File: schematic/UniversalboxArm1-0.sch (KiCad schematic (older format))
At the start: 170 parts, among them J1 USB_B_Micro, J110 Conn_01x03_Male, J120 Conn_02x04_Counter_Clockwise, J121 Conn_01x02_Male, J20 AVR-ISP-6, J50 Conn_01x14_Female, J60 Conn_01x06_Female, J61 Conn_02x08_Odd_Even, J62 Conn_02x04_Odd_Even, J90 Conn_02x03_Odd_Even, J91 Conn_02x04_Odd_Even, K90 IM01, K91 IM01, K92 IM01, K93 IM01, Q120 IRLML6402, Q20 BCX56-16, Q21 BSS138, Q22 BSS138, Q23 IRLML6402, Q24 IRLML6402, Q25 BSS138, Q50 IRLML6402, Q51 IRLML6402, Q60 BSS138, Q61 BSS138, Q62 BSS138, Q90 BSS138, Q91 BSS138, Q92 BSS138, Q93 BSS138, SW60 SW_SPST, SW61 SW_SPST, SW62 SW_SPST, SW63 SW_SPST, U1 USBLC6-2SC6, U110 MAX3221, U130 TSOP312xx, U2 LP38693MP-3.3, U20 ATtiny861A-SU, U21 REF3020, U22 MCP6542, U50 AT45DB641-S, U60 STM32L452RETx, U61 MCP65R41T-1202E, Y60 16MHz, Y61 32768Hz

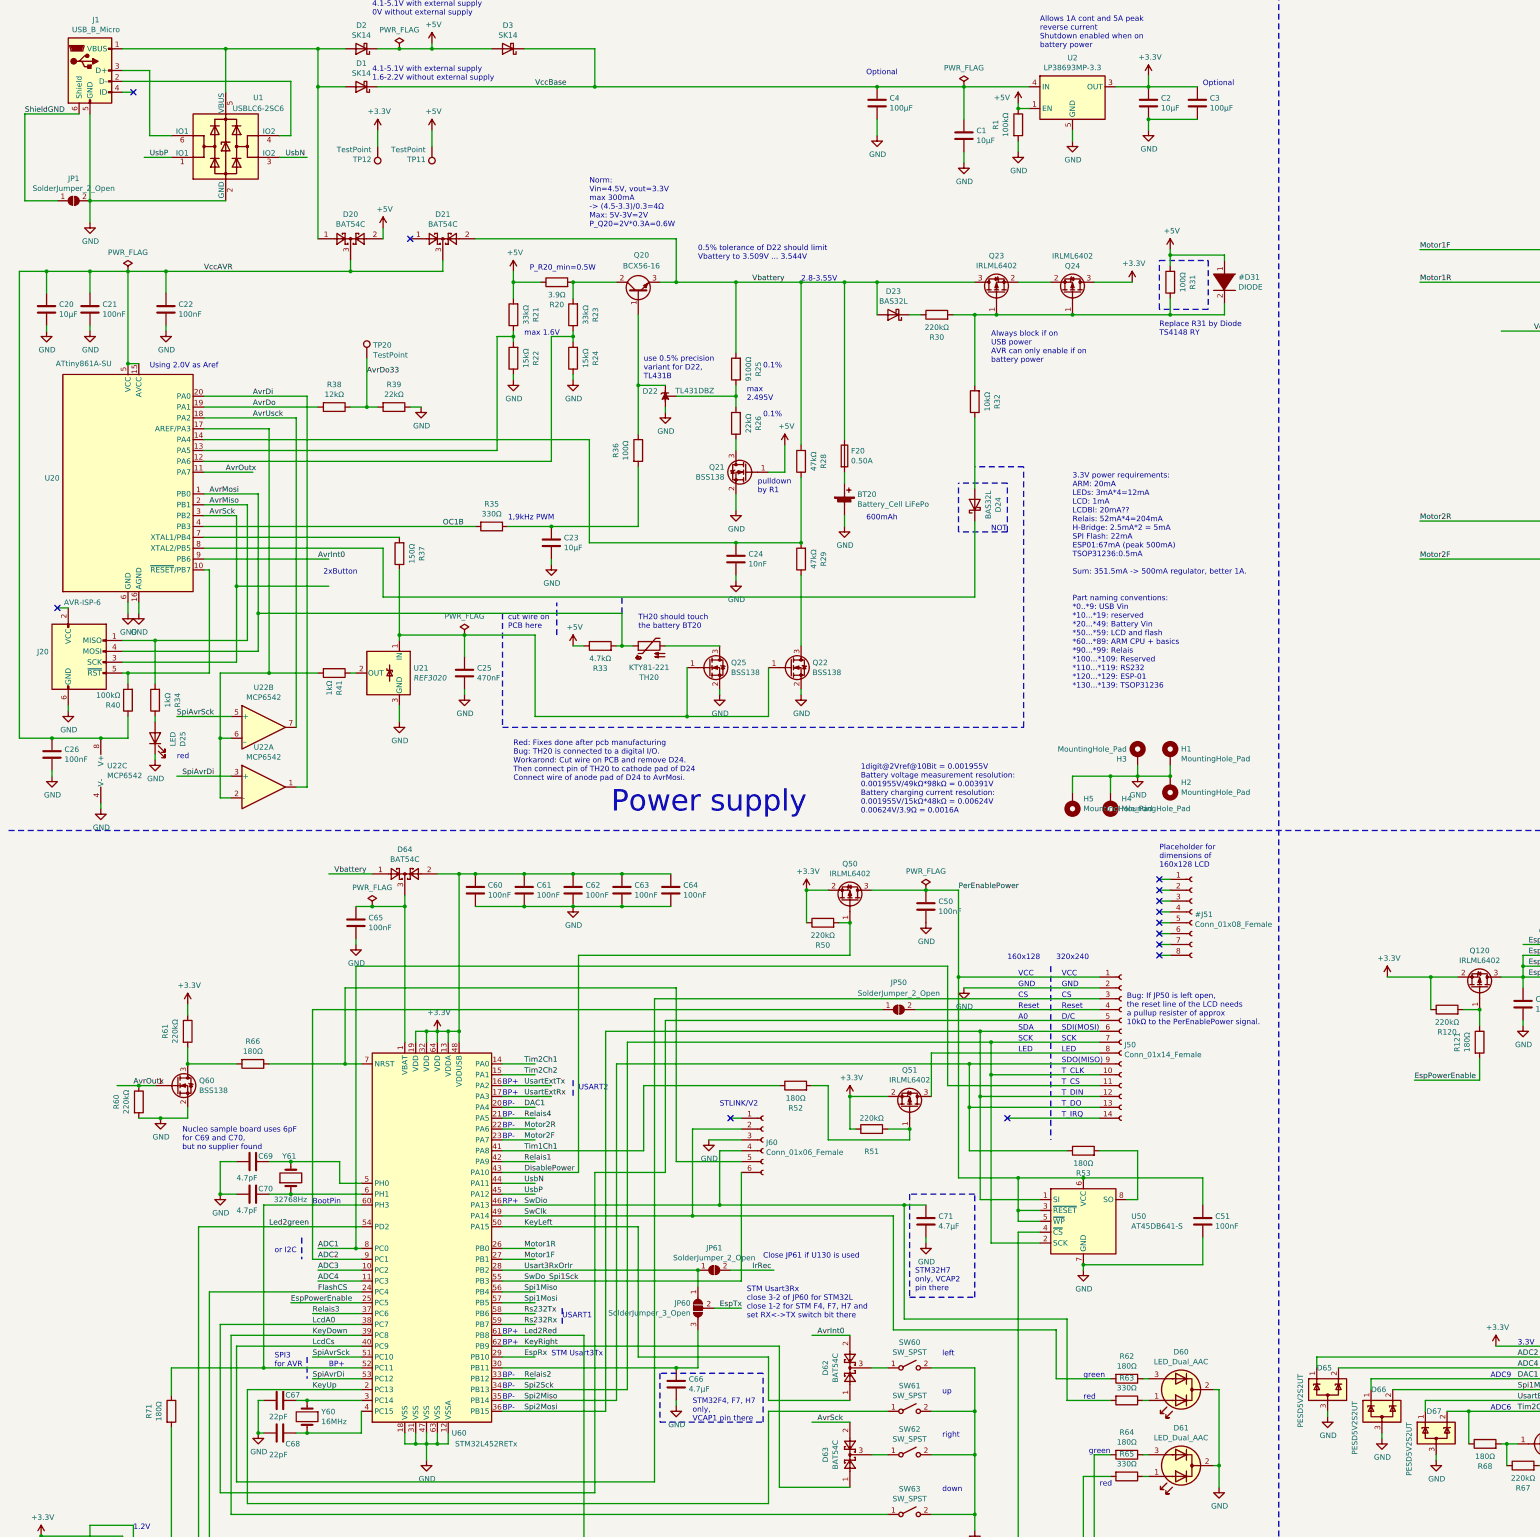
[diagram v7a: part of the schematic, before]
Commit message: Schematic: Revision 0.8 Workaround for issues with the crystals Reduce the value of two resistors
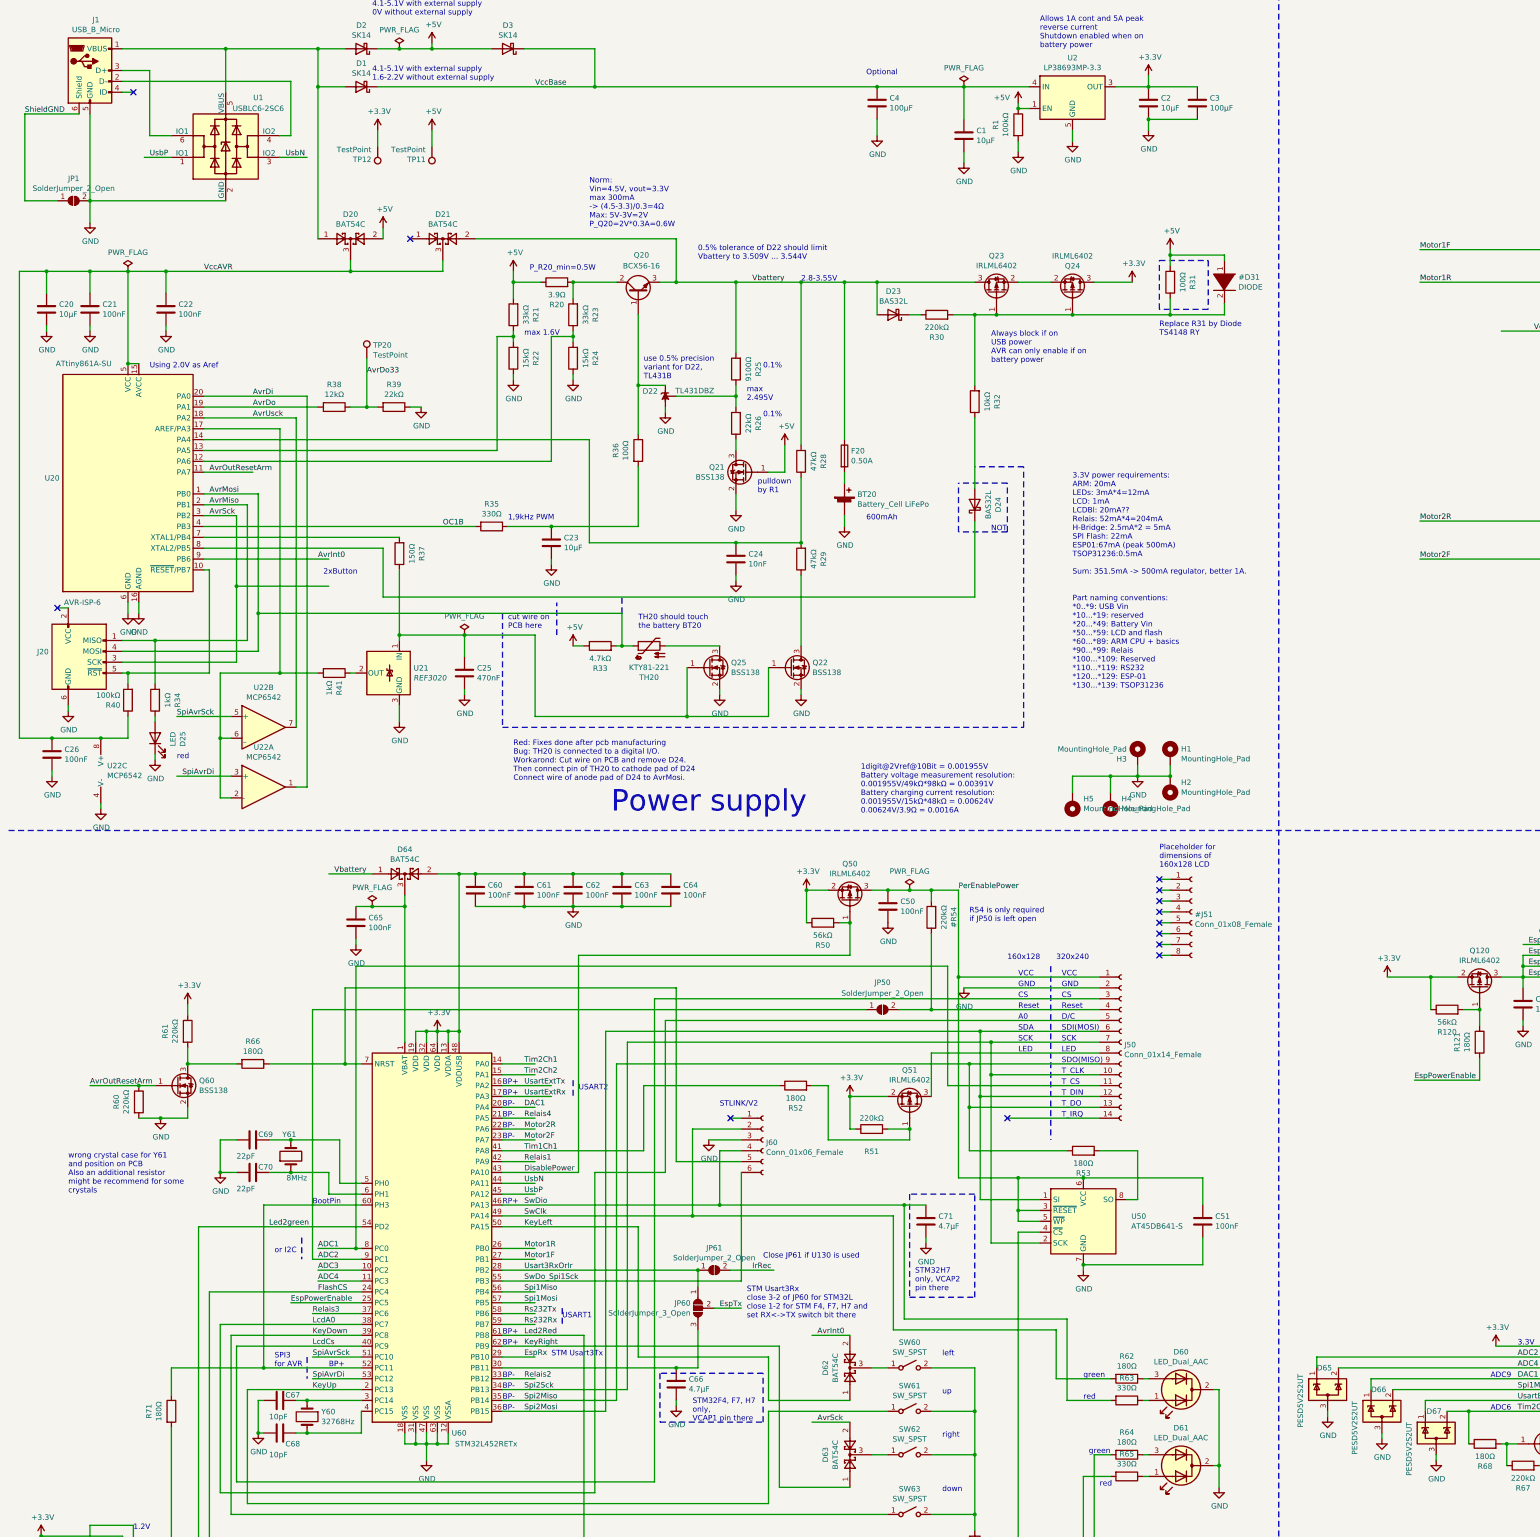
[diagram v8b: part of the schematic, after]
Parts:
- C67, C68: value 22pF -> 10pF
- C69, C70: value 4.7pF -> 22pF
- R120, R50: value 220kΩ -> 56kΩ
- Y60: value 16MHz -> 32768Hz
- Y61: value 32768Hz -> 8MHz
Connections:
- net labels added: 220kΩ, AvrOutResetArm
- net labels removed: AvrOutx
- wire segments 758 -> 765
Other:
- note added: "R54 is only required \nif JP50 is left open"
- note added: "wrong crystal case for Y61\nand position on PCB\nAlso an additional resistor\nmight be recommend for some\ncrystals"
- note removed: "Bug: If JP50 is left open,\nthe reset line of the LCD needs\na pullup resister of approx\n10kΩ to the PerEnablePower signal."
- note removed: "Nucleo sample board uses 6pF\nfor C69 and C70,\nbut no supplier found"
- moved on the sheet: C50, C69, C70, JP50, Y61
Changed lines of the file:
@@
 Sheet 1 1
 Title ""
-Date "2022-01-02"
-Rev "0.7"
+Date "2022-01-17"
+Rev "0.8"
 Comp ""
 Comment1 ""
@@
 	4700 7000 4700 6950
 Wire Wire Line
-	2900 6800 2900 4550
-Wire Wire Line
-	2300 4550 2900 4550
-Wire Wire Line
 	2350 5850 2350 6800
 Wire Wire Line
@@
 Wire Wire Line
 	2300 4950 2750 4950
-Text Label 2500 4950 0    50   ~ 0
-AvrOutx
+Text Label 2350 4950 0    50   ~ 0
+AvrOutResetArm
 $Comp
 L Connector:TestPoint TP20
@@
 $EndComp
 Wire Wire Line
-	3350 6800 2900 6800
+	3350 6800 3000 6800
 NoConn ~ 1650 1450
 Wire Wire Line
@@
 	2450 7400 2550 7400
 Wire Wire Line
-	2900 6800 2450 6800
-Wire Wire Line
 	2450 6800 2450 7400
-Connection ~ 2900 6800
 Connection ~ 2450 7400
 Text Label 2050 7200 0    50   ~ 0
@@
 Wire Wire Line
 	1850 10600 1700 10600
-Text Label 1650 10600 0    50   ~ 0
-AvrOutx
+Text Label 1250 10600 0    50   ~ 0
+AvrOutResetArm
 $Comp
 L Device:R R61
@@
 Connection ~ 1700 10600
 Wire Wire Line
-	1700 10600 1500 10600
-Wire Wire Line
 	2150 10800 2150 10900
 Wire Wire Line
@@
 P 3250 13650
 F 0 "Y60" V 3204 13781 50  0000 L CNN
-F 1 "16MHz" V 3295 13781 50  0000 L CNN
+F 1 "32768Hz" V 3295 13781 50  0000 L CNN
 F 2 "Crystal:Crystal_HC49-U_Vertical" H 3250 13650 50  0001 C CNN
 F 3 "~" H 3250 13650 50  0001 C CNN
@@
 P 3000 13500
 F 0 "C67" V 2950 13550 50  0000 L CNN
-F 1 "22pF" V 3150 13400 50  0000 L CNN
+F 1 "10pF" V 3150 13400 50  0000 L CNN
 F 2 "Capacitor_SMD:C_0805_2012Metric_Pad1.15x1.40mm_HandSolder" H 3038 13350 50  0001 C CNN
 F 3 "~" H 3000 13500 50  0001 C CNN
@@
 P 3000 13800
 F 0 "C68" V 3100 13850 50  0000 L CNN
-F 1 "22pF" V 3200 13700 50  0000 L CNN
+F 1 "10pF" V 3200 13700 50  0000 L CNN
 F 2 "Capacitor_SMD:C_0805_2012Metric_Pad1.15x1.40mm_HandSolder" H 3038 13650 50  0001 C CNN
 F 3 "~" H 3000 13800 50  0001 C CNN
@@
 	3750 11500 3550 11500
 Wire Wire Line
-	3550 11500 3550 11300
+	3550 11500 3550 11100
 $Comp
 L Device:C C69
 U 1 1 614F60AD
-P 2750 11300
-F 0 "C69" V 2700 11350 50  0000 L CNN
-F 1 "4.7pF" V 2900 11150 50  0000 L CNN
-F 2 "Capacitor_SMD:C_0805_2012Metric_Pad1.15x1.40mm_HandSolder" H 2788 11150 50  0001 C CNN
-F 3 "~" H 2750 11300 50  0001 C CNN
-	1    2750 11300
+P 2750 11100
+F 0 "C69" V 2700 11150 50  0000 L CNN
+F 1 "22pF" V 2900 10950 50  0000 L CNN
+F 2 "Capacitor_SMD:C_0805_2012Metric_Pad1.15x1.40mm_HandSolder" H 2788 10950 50  0001 C CNN
+F 3 "~" H 2750 11100 50  0001 C CNN
+	1    2750 11100
 	0    1    1    0
 $EndComp
@@
 L Device:C C70
 U 1 1 614F6223
-P 2750 11600
-F 0 "C70" V 2700 11650 50  0000 L CNN
-F 1 "4.7pF" V 2900 11450 50  0000 L CNN
-F 2 "Capacitor_SMD:C_0805_2012Metric_Pad1.15x1.40mm_HandSolder" H 2788 11450 50  0001 C CNN
-F 3 "~" H 2750 11600 50  0001 C CNN
-	1    2750 11600
+P 2750 11400
+F 0 "C70" V 2700 11450 50  0000 L CNN
+F 1 "22pF" V 2900 11250 50  0000 L CNN
+F 2 "Capacitor_SMD:C_0805_2012Metric_Pad1.15x1.40mm_HandSolder" H 2788 11250 50  0001 C CNN
+F 3 "~" H 2750 11400 50  0001 C CNN
+	1    2750 11400
 	0    1    1    0
 $EndComp
 Wire Wire Line
-	2600 11600 2450 11600
+	2600 11400 2450 11400
 Wire Wire Line
-	2450 11600 2450 11300
+	2450 11400 2450 11100
 Wire Wire Line
-	2450 11300 2600 11300
+	2450 11100 2600 11100
 $Comp
 L power:GND #PWR0173
 U 1 1 615D30F6
-P 2450 11600
-F 0 "#PWR0173" H 2450 11350 50  0001 C CNN
-F 1 "GND" H 2455 11427 50  0000 C CNN
-F 2 "" H 2450 11600 50  0001 C CNN
-F 3 "" H 2450 11600 50  0001 C CNN
-	1    2450 11600
+P 2450 11400
+F 0 "#PWR0173" H 2450 11150 50  0001 C CNN
+F 1 "GND" H 2455 11227 50  0000 C CNN
+F 2 "" H 2450 11400 50  0001 C CNN
+F 3 "" H 2450 11400 50  0001 C CNN
+	1    2450 11400
 	1    0    0    -1
 $EndComp
-Connection ~ 2450 11600
+Connection ~ 2450 11400
 Connection ~ 3250 13500
 Wire Wire Line
@@
 $EndComp
 Wire Wire Line
-	8450 8800 8950 8800
+	8450 8800 8600 8800
 $Comp
 L Device:C C50
 U 1 1 60E5A73A
-P 8950 8950
-F 0 "C50" H 9065 8996 50  0000 L CNN
-F 1 "100nF" H 9065 8905 50  0000 L CNN
-F 2 "Capacitor_SMD:C_0805_2012Metric_Pad1.15x1.40mm_HandSolder" H 8988 8800 50  0001 C CNN
-F 3 "~" H 8950 8950 50  0001 C CNN
-	1    8950 8950
+P 8600 8950
+F 0 "C50" H 8715 8996 50  0000 L CNN
+F 1 "100nF" H 8715 8905 50  0000 L CNN
+F 2 "Capacitor_SMD:C_0805_2012Metric_Pad1.15x1.40mm_HandSolder" H 8638 8800 50  0001 C CNN
+F 3 "~" H 8600 8950 50  0001 C CNN
+	1    8600 8950
 	1    0    0    -1
 $EndComp
@@
 L power:GND #PWR0181
 U 1 1 60E5BD97
-P 8950 9100
-F 0 "#PWR0181" H 8950 8850 50  0001 C CNN
-F 1 "GND" H 8955 8927 50  0000 C CNN
-F 2 "" H 8950 9100 50  0001 C CNN
-F 3 "" H 8950 9100 50  0001 C CNN
-	1    8950 9100
+P 8600 9100
+F 0 "#PWR0181" H 8600 8850 50  0001 C CNN
+F 1 "GND" H 8605 8927 50  0000 C CNN
+F 2 "" H 8600 9100 50  0001 C CNN
+F 3 "" H 8600 9100 50  0001 C CNN
+	1    8600 9100
 	1    0    0    -1
 $EndComp
@@
 	1    0    0    -1
 $EndComp
-Connection ~ 8950 8800
 Wire Wire Line
 	7050 11700 8750 11700
@@
 P 8000 9100
 F 0 "R50" V 7793 9100 50  0000 C CNN
-F 1 "220kΩ" V 7884 9100 50  0000 C CNN
+F 1 "56kΩ" V 7884 9100 50  0000 C CNN
 F 2 "Resistor_SMD:R_0805_2012Metric_Pad1.15x1.40mm_HandSolder" V 7930 9100 50  0001 C CNN
 F 3 "~" H 8000 9100 50  0001 C CNN
@@
 L power:PWR_FLAG #FLG0107
 U 1 1 631292F2
-P 8950 8800
-F 0 "#FLG0107" H 8950 8875 50  0001 C CNN
-F 1 "PWR_FLAG" H 8950 8974 50  0000 C CNN
-F 2 "" H 8950 8800 50  0001 C CNN
-F 3 "~" H 8950 8800 50  0001 C CNN
-	1    8950 8800
+P 8800 8800
+F 0 "#FLG0107" H 8800 8875 50  0001 C CNN
+F 1 "PWR_FLAG" H 8800 8974 50  0000 C CNN
+F 2 "" H 8800 8800 50  0001 C CNN
+F 3 "~" H 8800 8800 50  0001 C CNN
+	1    8800 8800
 	1    0    0    -1
 $EndComp
@@
 P 13750 9900
 F 0 "R120" V 13543 9900 50  0000 C CNN
-F 1 "220kΩ" V 13634 9900 50  0000 C CNN
+F 1 "56kΩ" V 13634 9900 50  0000 C CNN
 F 2 "Resistor_SMD:R_0805_2012Metric_Pad1.15x1.40mm_HandSolder" V 13680 9900 50  0001 C CNN
 F 3 "~" H 13750 9900 50  0001 C CNN
@@
 Wire Wire Line
 	9250 9600 9250 8800
-Wire Wire Line
-	9250 8800 8950 8800
 $Comp
 L Connector:Conn_01x02_Male J121
@@
 L Jumper:SolderJumper_2_Open JP50
 U 1 1 60FE0A28
-P 8700 9900
-F 0 "JP50" H 8700 10150 50  0000 C CNN
-F 1 "SolderJumper_2_Open" H 8700 10050 50  0000 C CNN
-F 2 "Jumper:SolderJumper-2_P1.3mm_Open_RoundedPad1.0x1.5mm" H 8700 9900 50  0001 C CNN
-F 3 "~" H 8700 9900 50  0001 C CNN
-	1    8700 9900
+P 8550 9900
+F 0 "JP50" H 8550 10150 50  0000 C CNN
+F 1 "SolderJumper_2_Open" H 8550 10050 50  0000 C CNN
+F 2 "Jumper:SolderJumper-2_P1.3mm_Open_RoundedPad1.0x1.5mm" H 8550 9900 50  0001 C CNN
+F 3 "~" H 8550 9900 50  0001 C CNN
+	1    8550 9900
 	1    0    0    -1
 $EndComp
 Wire Wire Line
-	8850 9900 10550 9900
+	8700 9900 9000 9900
 Wire Wire Line
-	8550 9900 3300 9900
+	8400 9900 3300 9900
 Wire Wire Line
 	3750 12500 2350 12500
@@
 Text Notes 7450 4450 0    50   ~ 0
 0.1%
-Text Notes 2100 11200 0    50   ~ 0
-Nucleo sample board uses 6pF\nfor C69 and C70,\nbut no supplier found
 $Comp
 L power:+5V #PWR0204
@@
 	10650 7750 10650 7900
 Wire Wire Line
-	2900 11600 3100 11600
-Wire Wire Line
-	2900 11300 3100 11300
-Connection ~ 3100 11600
+	2900 11400 3100 11400
 Wire Wire Line
-	3100 11600 3750 11600
-Connection ~ 3100 11300
+	2900 11100 3100 11100
+Connection ~ 3100 11400
+Connection ~ 3100 11100
 Wire Wire Line
-	3100 11300 3550 11300
+	3100 11100 3550 11100
 $Comp
 L Jumper:SolderJumper_2_Open JP61
@@
 	11450 1700 11000 1700
 Connection ~ 11000 1700
-Text Notes 11500 1400 0    50   ~ 0
-Optional
 $Comp
 L Device:C C4
@@
 L Device:Crystal Y61
 U 1 1 6146543E
-P 3100 11450
-F 0 "Y61" V 3300 11400 50  0000 L CNN
-F 1 "32768Hz" V 2900 11300 50  0000 L CNN
-F 2 "MalteM:Crystal_MP03" H 3100 11450 50  0001 C CNN
-F 3 "~" H 3100 11450 50  0001 C CNN
-	1    3100 11450
+P 3100 11250
+F 0 "Y61" V 3300 11200 50  0000 L CNN
+F 1 "8MHz" V 2900 11100 50  0000 L CNN
+F 2 "MalteM:Crystal_MP03" H 3100 11250 50  0001 C CNN
+F 3 "~" H 3100 11250 50  0001 C CNN
+	1    3100 11250
 	0    -1   -1   0
 $EndComp
@@
 Text Notes 5050 11700 0    50   ~ 0
 RP+
-Text Notes 10800 10050 0    50   ~ 0
-Bug: If JP50 is left open,\nthe reset line of the LCD needs\na pullup resister of approx\n10kΩ to the PerEnablePower signal.
+Text Notes 9350 9100 0    50   ~ 0
+R54 is only required \nif JP50 is left open
+Text Notes 1050 11600 0    50   ~ 0
+wrong crystal case for Y61\nand position on PCB\nAlso an additional resistor\nmight be recommend for some\ncrystals
+Wire Wire Line
+	3100 11400 3450 11400
+Wire Wire Line
+	3450 11400 3450 11600
+Wire Wire Line
+	3450 11600 3750 11600
+Wire Wire Line
+	1250 10600 1700 10600
+Wire Wire Line
+	3000 4550 3000 6800
+Connection ~ 3000 6800
+Wire Wire Line
+	2450 6800 3000 6800
+Wire Wire Line
+	2300 4550 3000 4550
+$Comp
+L Device:R #R54
+U 1 1 620B0931
+P 9000 9050
+F 0 "#R54" V 8793 9050 50  0000 C CNN
+F 1 "220kΩ" V 8884 9050 50  0000 C CNN
+F 2 "Resistor_SMD:R_0805_2012Metric_Pad1.15x1.40mm_HandSolder" V 8930 9050 50  0001 C CNN
+F 3 "~" H 9000 9050 50  0001 C CNN
+	1    9000 9050
+	-1   0    0    1
+$EndComp
+Connection ~ 8600 8800
+Wire Wire Line
+	8600 8800 8800 8800
+Connection ~ 8800 8800
+Wire Wire Line
+	8800 8800 9000 8800
+Wire Wire Line
+	9000 8900 9000 8800
+Connection ~ 9000 8800
+Wire Wire Line
+	9000 8800 9250 8800
+Wire Wire Line
+	9000 9200 9000 9900
+Connection ~ 9000 9900
+Wire Wire Line
+	9000 9900 10550 9900
 $EndSCHEMATC
